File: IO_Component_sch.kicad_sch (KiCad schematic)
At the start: 21 parts

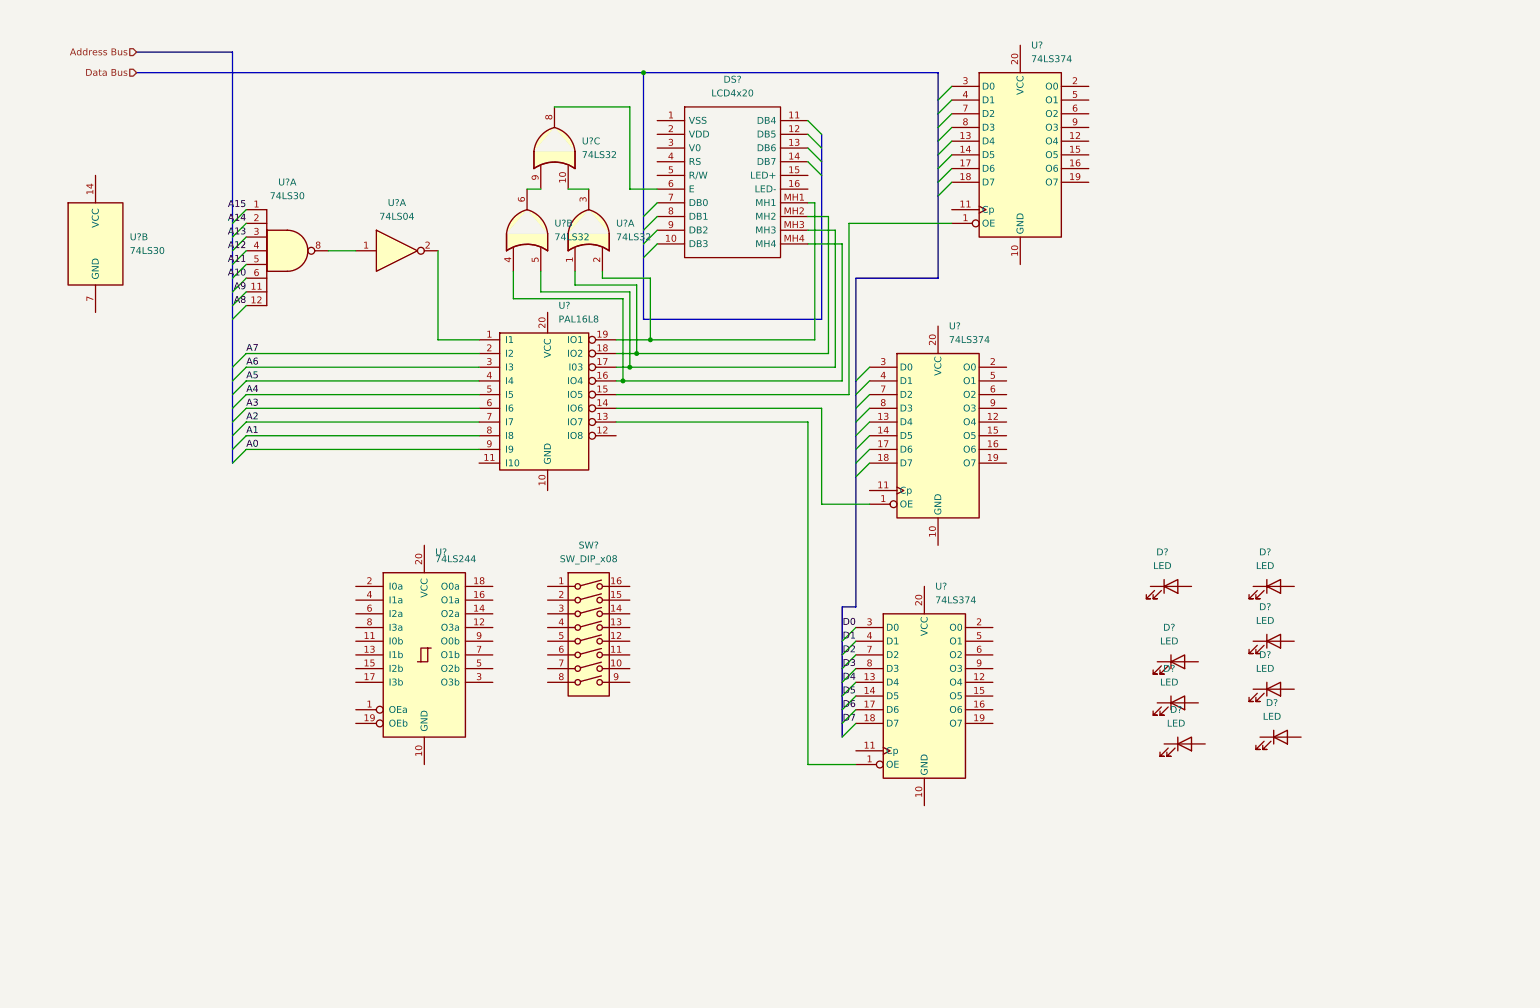
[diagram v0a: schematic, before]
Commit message: Finished wiring and decoding IO devices (except for push button switches)
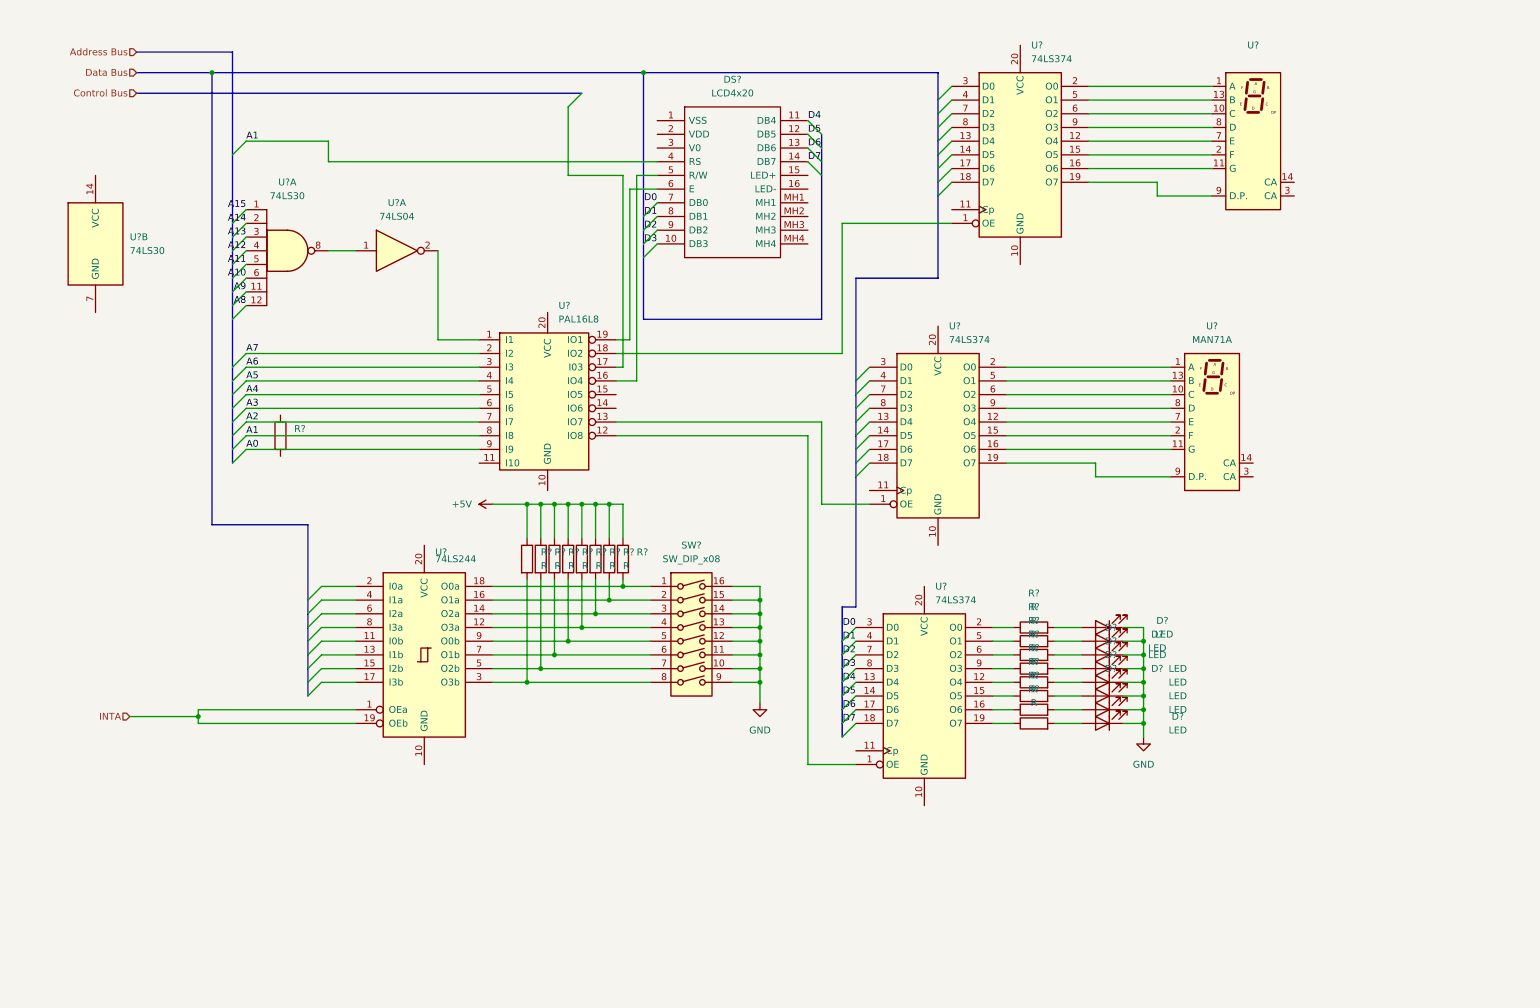
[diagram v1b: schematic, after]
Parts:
- removed U? (x3): 74LS32, symbol 74xx:74LS32
- added R? (x15): R, symbol Device:R
- added R? (x2): (no value), symbol Device:R
- added U?: (no value), symbol Display_Character:MAN71A
- added U?: MAN71A, Display_7Segment:MAN71A, symbol Display_Character:MAN71A
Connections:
- net A1: now also DS?.4 (RS)
- net D0: now also DS?.7 (DB0)
- net D1: now also DS?.8 (DB1)
- net D2: now also DS?.9 (DB2)
- net D3: now also DS?.10 (DB3)
- net D4: now also DS?.11 (DB4)
- net D5: now also DS?.12 (DB5)
- net D6: now also DS?.13 (DB6)
- net D7: now also DS?.14 (DB7)
- net at U?.1 (OE): now also U?.18 (IO2); no longer U?.15 (IO5)
- net at U?.12 (O4): now also U?.7 (E) (x2)
- net at U?.15 (O5): now also U?.2 (F) (x2)
- net at U?.16 (O6): now also U?.11 (G) (x2)
- net at U?.19 (O7): now also U?.9 (D.P.) (x2)
- net at U?.2 (O0): now also U?.1 (A) (x2)
- net at U?.5 (O1): now also U?.13 (B) (x2)
- net at U?.6 (O2): now also U?.10 (C) (x2)
- net at U?.9 (O3): now also U?.8 (D) (x2)
- net at DS?.6 (E): now also U?.19 (IO1)
- net GND: now reaches D?.1 (K)
- net GND: now also D?.1 (K), D?.1 (K), D?.1 (K), D?.1 (K), D?.1 (K), D?.1 (K), D?.1 (K), SW?.10, SW?.11, SW?.12, SW?.13, SW?.14, SW?.15, SW?.16, SW?.9
- net at D?.2 (A): now also R?.2 (x8)
- net at U?.16 (IO4): now also DS?.5 (R/W); no longer DS?.MH4
- net at U?.17 (I03): no longer DS?.MH3
- net at U?.1 (OE): now also U?.13 (IO7); no longer U?.14 (IO6)
- net at U?.1 (OE): now also U?.12 (IO8); no longer U?.13 (IO7)
- net at U?.12 (O4): now also R?.1
- net at U?.15 (O5): now also R?.1
- net at U?.16 (O6): now also R?.1
- net at U?.19 (O7): now also R?.1
- net at U?.2 (O0): now also R?.1
- net at U?.5 (O1): now also R?.1
- net at U?.6 (O2): now also R?.1
- net at U?.9 (O3): now also R?.1
- net at DS?.MH2: no longer U?.18 (IO2)
- net at DS?.MH1: no longer U?.19 (IO1)
- net INTA: now reaches U?.1 (OEa)
- net INTA: now also U?.19 (OEb)
- net at U?.12 (O3a): now also SW?.4, R?.2
- net at U?.14 (O2a): now also SW?.3, R?.2
- net at U?.16 (O1a): now also SW?.2, R?.2
- net at U?.18 (O0a): now also SW?.1, R?.2
- net at U?.3 (O3b): now also SW?.8, R?.2
- net at U?.5 (O2b): now also SW?.7, R?.2
- net at U?.7 (O1b): now also SW?.6, R?.2
- net at U?.9 (O0b): now also SW?.5, R?.2
- new net +5V: R?.1, R?.1, R?.1, R?.1, R?.1, R?.1, R?.1, R?.1
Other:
- moved on the sheet: D?, SW?

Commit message: Wired Push Buttons and added footprints
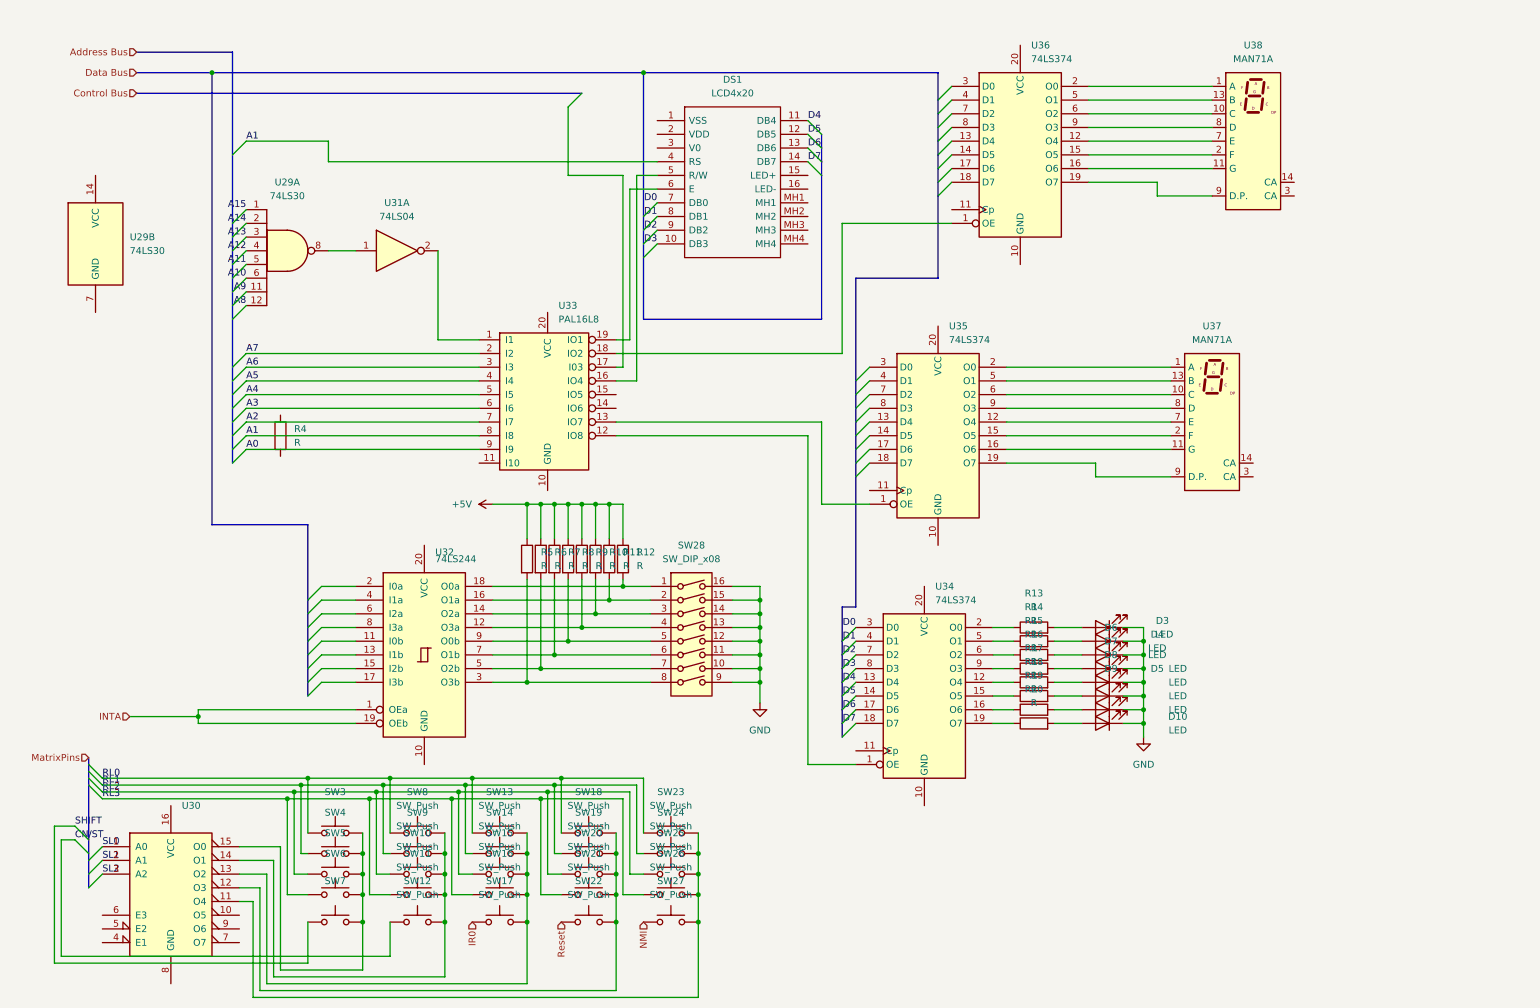
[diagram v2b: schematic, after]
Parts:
- added SW10, SW11, SW12, SW13, SW14, SW15, SW16, SW17, SW18, SW19, SW20, SW21, SW22, SW23, SW24, SW25, SW26, SW27, SW8, SW9: SW_Push, symbol Switch:SW_Push
- added SW3, SW4, SW5, SW6, SW7: (no value), symbol Switch:SW_Push
- added U30: (no value), symbol 74xx:74LS138
- DS1: renamed from DS?; footprint LCD4x20 -> (none)
- R12, R4: renamed from R?; value (none) -> R
- U38: renamed from U?; value (none) -> MAN71A; footprint (none) -> Display_7Segment:MAN71A
- gave numbers to parts that had none: 32
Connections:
- new net: SW10.2, SW11.2, SW12.2, SW8.2, SW9.2, U30.14 (O1)
- new net: SW18.2, SW19.2, SW20.2, SW21.2, SW22.2, U30.12 (O3)
- new net: SW23.2, SW24.2, SW25.2, SW26.2, SW27.2, U30.11 (O4)
- new net: SW13.2, SW14.2, SW15.2, SW16.2, SW17.2, U30.13 (O2)
- new net: SW3.2, SW4.2, SW5.2, SW6.2, SW7.2, U30.15 (O0)
- new net CN/ST: SW12.1
- new net IR0: SW17.1
- new net NMI: SW27.1
- new net RL0: SW13.1, SW18.1, SW23.1, SW3.1, SW8.1
- new net RL1: SW14.1, SW19.1, SW24.1, SW4.1, SW9.1
- new net RL2: SW10.1, SW15.1, SW20.1, SW25.1, SW5.1
- new net RL3: SW11.1, SW16.1, SW21.1, SW26.1, SW6.1
- new net Reset: SW22.1
- new net SHIFT: SW7.1
- new net SL0: U30.1 (A0)
- new net SL1: U30.2 (A1)
- new net SL2: U30.3 (A2)

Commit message: Added power and ground to chips
Added power and ground to chips as well as checked and added all labels for pins off of busses
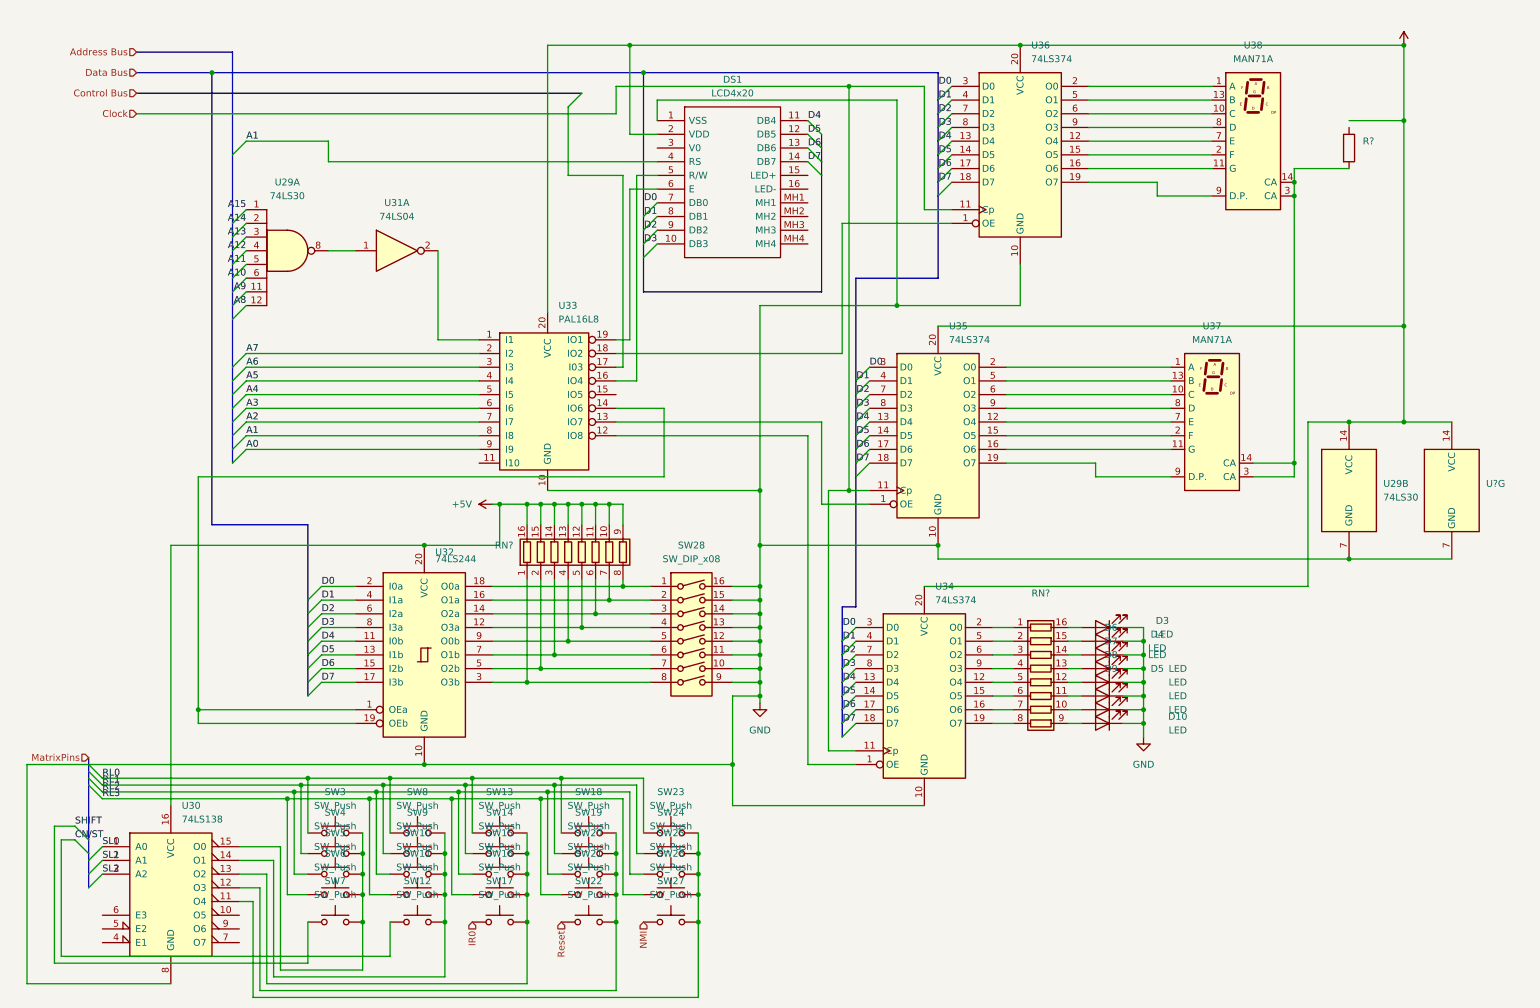
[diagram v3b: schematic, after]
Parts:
- removed R10, R11, R12, R13, R14, R15, R16, R17, R18, R19, R20, R4, R5, R6, R7, R8, R9: R, symbol Device:R
- added R?: (no value), symbol Device:R
- added RN? (x2): (no value), symbol Device:R_Pack08
- added U?: (no value), symbol 74xx:74LS04
- D10, D3, D4, D5, D6, D7, D8, D9: footprint (none) -> LED_SMD:LED_0201_0603Metric
- DS1: footprint (none) -> parts:LCD4x20
- SW10, SW11, SW12, SW13, SW14, SW15, SW16, SW17, SW18, SW19, SW20, SW21, SW22, SW23, SW24, SW25, SW26, SW27, SW8, SW9: footprint (none) -> Button_Switch_Keyboard:SW_Cherry_MX_1.00u_PCB
- SW28: footprint (none) -> Connector_DIN:DIN41612_D_2x8_Female_Vertical_THT
- SW3, SW4, SW5, SW6, SW7: value (none) -> SW_Push; footprint (none) -> Button_Switch_Keyboard:SW_Cherry_MX_1.00u_PCB
- U29: footprint (none) -> Package_DIP:PowerIntegrations_eDIP-12B
- U30: value (none) -> 74LS138; footprint (none) -> Package_DIP:DIP-16_W7.62mm
- U31: footprint (none) -> Package_DIP:DIP-14_W7.62mm
- U32, U33, U34, U35, U36: footprint (none) -> Package_DIP:DIP-20_W7.62mm
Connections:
- net INTA is gone; now on an unnamed net: U32.1 (OEa), U32.19 (OEb)
- net +5V: now also DS1.2 (VDD), U29.14 (VCC), U30.16 (VCC), U32.20 (VCC), U33.20 (VCC), U34.20 (VCC), U35.20 (VCC), U36.20 (VCC), RN?.10 (R7.2), RN?.11 (R6.2), RN?.12 (R5.2), RN?.13 (R4.2), RN?.14 (R3.2), RN?.15 (R2.2), RN?.16 (R1.2), RN?.9 (R8.2), U?.14 (VCC)
- net D0: now also U32.2 (I0a), U35.3 (D0), U36.3 (D0)
- net D1: now also U32.4 (I1a), U35.4 (D1), U36.4 (D1)
- net D2: now also U32.6 (I2a), U35.7 (D2), U36.7 (D2)
- net D3: now also U32.8 (I3a), U35.8 (D3), U36.8 (D3)
- net D4: now also U32.11 (I0b), U35.13 (D4), U36.13 (D4)
- net D5: now also U32.13 (I1b), U35.14 (D5), U36.14 (D5)
- net D6: now also U32.15 (I2b), U35.17 (D6), U36.17 (D6)
- net D7: now also U32.17 (I3b), U35.18 (D7), U36.18 (D7)
- net GND: now also DS1.1 (VSS), U29.7 (GND), U30.8 (GND), U32.10 (GND), U33.10 (GND), U34.10 (GND), U35.10 (GND), U36.10 (GND), U?.7 (GND)
- net Clock: now reaches U36.11 (Cp)
- net Clock: now also U34.11 (Cp), U35.11 (Cp)
- net at U34.9 (O3): now also RN?.4 (R4.1)
- net at D6.2 (A): now also RN?.13 (R4.2)
- net at D10.2 (A): now also RN?.9 (R8.2)
- net at SW28.3, U32.14 (O2a): now also RN?.6 (R6.1)
- net at SW28.7, U32.5 (O2b): now also RN?.2 (R2.1)
- net at U34.15 (O5): now also RN?.6 (R6.1)
- net at D8.2 (A): now also RN?.11 (R6.2)
- net at U38.12 (NC): now also U37.14 (CA), U37.3 (CA), U38.14 (CA), U38.3 (CA), R?.2
- net at U34.12 (O4): now also RN?.5 (R5.1)
- net at D7.2 (A): now also RN?.12 (R5.2)
- net at SW28.1, U32.18 (O0a): now also RN?.8 (R8.1)
- net at U34.16 (O6): now also RN?.7 (R7.1)
- net at U34.19 (O7): now also RN?.8 (R8.1)
- net at U34.2 (O0): now also RN?.1 (R1.1)
- net at U34.5 (O1): now also RN?.2 (R2.1)
- net at U34.6 (O2): now also RN?.3 (R3.1)
- net at SW28.4, U32.12 (O3a): now also RN?.5 (R5.1)
- net at SW28.5, U32.9 (O0b): now also RN?.4 (R4.1)
- net at D3.2 (A): now also RN?.16 (R1.2)
- net at SW28.6, U32.7 (O1b): now also RN?.3 (R3.1)
- net at D4.2 (A): now also RN?.15 (R2.2)
- net at SW28.2, U32.16 (O1a): now also RN?.7 (R7.1)
- net at D5.2 (A): now also RN?.14 (R3.2)
- net at D9.2 (A): now also RN?.10 (R7.2)
- net at SW28.8, U32.3 (O3b): now also RN?.1 (R1.1)
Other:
- moved on the sheet: U29B
